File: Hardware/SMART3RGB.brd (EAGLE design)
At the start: 40 x 54 mm, 14 parts, among them IC1 WS2811-SOP8, IC2 WS2811-SOP8, IC3 WS2811-SOP8, IC4 WS2811-SOP8, SW1 QG16F-RGB, SW2 QG16F-RGB, SW3 QG16F-RGB, SW4 QG16F-RGB

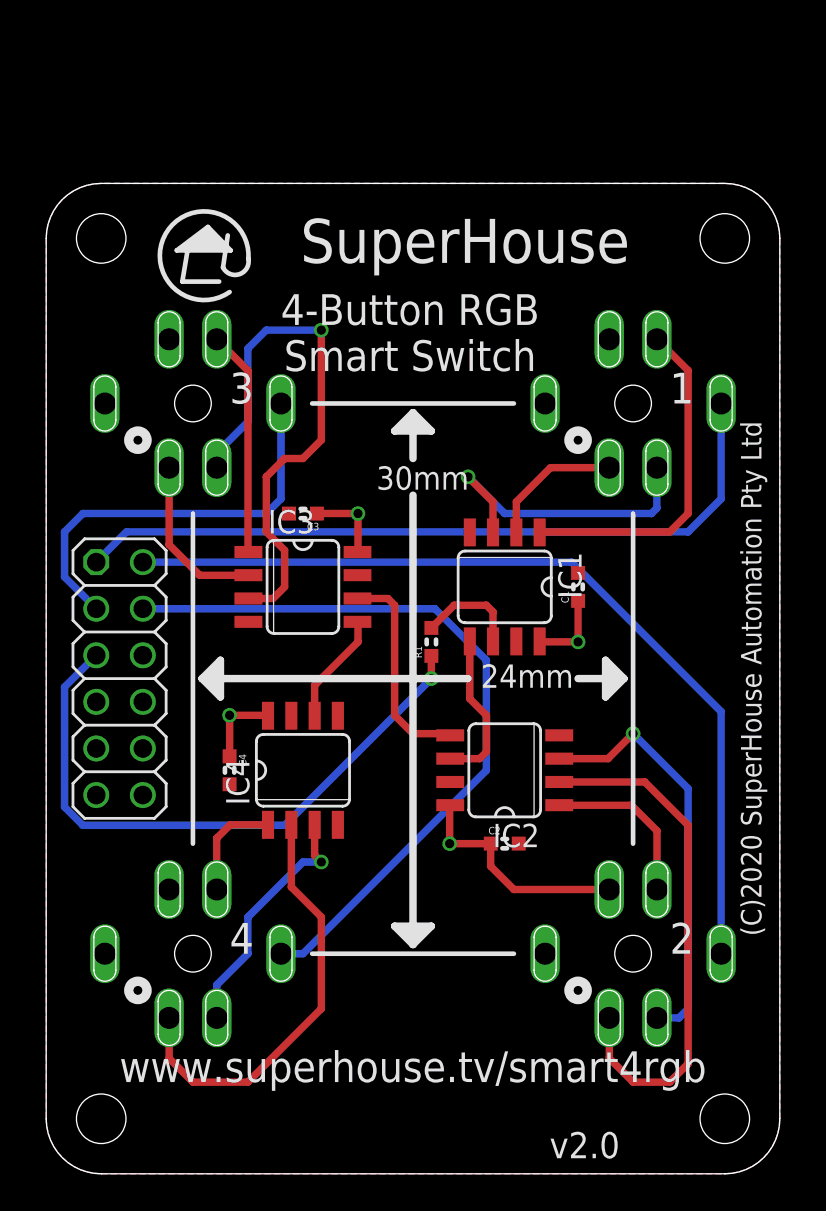
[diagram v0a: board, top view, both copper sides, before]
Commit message: Routing, ERC, and DRC for v2.0 release.
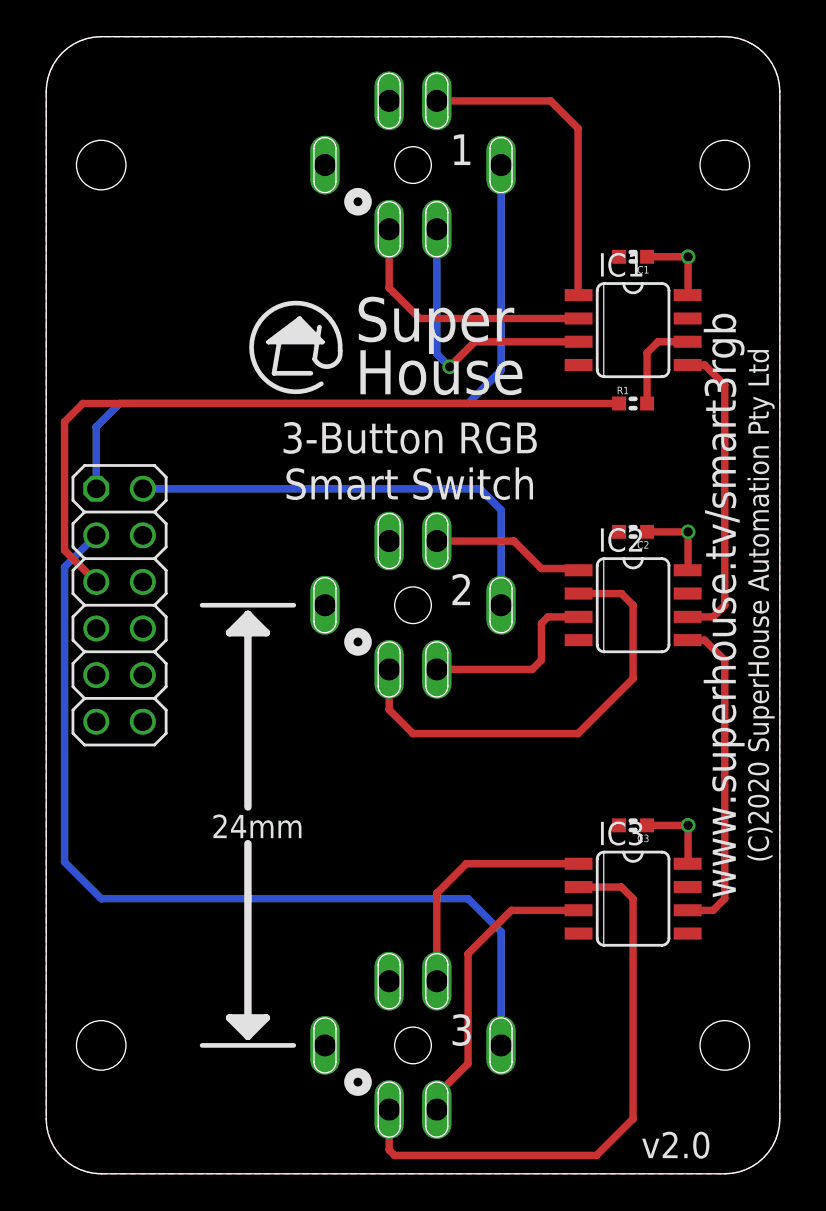
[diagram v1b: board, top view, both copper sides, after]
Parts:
- removed C4: 1uF, SuperHouse-DiscreteSemi:C0603
- removed IC4: WS2811-SOP8, SuperHouse-ICs:SO08-SKINNYPADS
- removed SW4: QG16F-RGB, SuperHouse-Switches:QG16F-RGB
- moved SW3 37.0 mm to (20.0, 7.00)
- moved C3 24.8 mm to (32.0, 19.0)
- moved IC3 24.8 mm to (32.0, 15.0)
- moved SW2 22.5 mm to (20.0, 31.0)
- moved C2 18.4 mm to (32.0, 35.0), turned to 180 degrees
- moved C1 18.2 mm to (32.0, 50.0), turned to 180 degrees
- moved SW1 17.7 mm to (20.0, 55.0)
- moved R1 17.0 mm to (32.0, 42.0), turned to 0 degrees
- moved IC1 15.7 mm to (32.0, 46.0), turned to 270 degrees
- moved IC2 11.4 mm to (32.0, 31.0), turned to 270 degrees
- moved H1 4.00 mm to (4.00, 31.0)
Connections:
- removed net LED4B: IC4.3, SW4.G
- removed net LED4G: IC4.2, SW4.B
- removed net LED4R: IC4.1, SW4.R
- removed net N$13: IC3.5, IC4.6
- net 5V: no longer C4.1, IC4.8, SW4.A
- net DATA_4: no longer SW4.1
- net GND: no longer C4.2, IC4.4, SW4.2
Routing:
- net DATA_4: track 41.2 -> 0.00 mm
- net DATA_3: track 22.7 -> 50.1 mm
- net LED4G: track 23.4 -> 0.00 mm
- net DATA_2: track 48.1 -> 25.2 mm
- net LED3G: track 9.22 -> 31.7 mm
- net LED3B: track 30.1 -> 16.2 mm, vias 1 -> 0
- net LED4B: track 13.6 -> 0.00 mm, vias 1 -> 0
- net 5V: track 25.7 -> 13.0 mm, vias 4 -> 3
- net LED2B: track 22.7 -> 10.1 mm, vias 1 -> 0
- net N$6: track 8.53 -> 16.8 mm
- net LED1G: track 7.50 -> 14.2 mm
- net DATA_5: track 34.0 -> 40.1 mm, vias 1 -> 0
- net N$13: track 6.11 -> 0.00 mm
- net N$12: track 11.7 -> 17.8 mm
- net LED4R: track 5.90 -> 0.00 mm
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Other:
- board size 40 x 54 mm -> 40 x 62 mm
- board text added: "3-Button RGB Smart Switch"
- board text added: "Super House"
- board text added: "www.superhouse.tv/smart3rgb"
- board text removed: "30mm"
- board text removed: "4"
- board text removed: "4-Button RGB Smart Switch"
- board text removed: "SuperHouse"
- board text removed: "www.superhouse.tv/smart4rgb"

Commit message: Converted switch isolation from FETs to diodes for v2.1 release.
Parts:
- moved C1 1.00 mm to (32.0, 51.0)
- moved C2 1.00 mm to (32.0, 36.0)
- moved C3 1.00 mm to (32.0, 20.0)
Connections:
- net LED1B: now also SW1.B; no longer SW1.G
- net LED1G: now also IC1.1, SW1.G; no longer IC1.2, SW1.B
- net LED1R: now also IC1.2; no longer IC1.1
- net LED2B: now also SW2.B; no longer SW2.G
- net LED2G: now also IC2.1, SW2.G; no longer IC2.2, SW2.B
- net LED2R: now also IC2.2; no longer IC2.1
- net LED3B: now also SW3.B; no longer SW3.G
- net LED3G: now also IC3.1, SW3.G; no longer IC3.2, SW3.B
- net LED3R: now also IC3.2; no longer IC3.1
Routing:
- net LED2G: track 24.5 -> 11.7 mm
- net LED2B: track 10.1 -> 22.6 mm
- net LED3G: track 31.7 -> 19.7 mm
- net LED3B: track 16.2 -> 26.2 mm
- net LED3R: track 13.2 -> 19.7 mm
- net LED2R: track 8.39 -> 13.4 mm
- net LED1R: track 17.4 -> 21.3 mm
- net LED1G: track 14.2 -> 10.9 mm
- net 5V: track 13.0 -> 14.3 mm
- net LED1B: track 15.4 -> 14.7 mm, vias 1 -> 0
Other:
- board text added: "v2.1"
- board text removed: "v2.0"
